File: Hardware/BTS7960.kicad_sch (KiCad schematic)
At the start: 29 parts, among them J10 Screw_Terminal_01x04, J11 Screw_Terminal_01x04, J4 Screw_Terminal_01x04, U7 HCPL-2631, U8 HCPL-2631

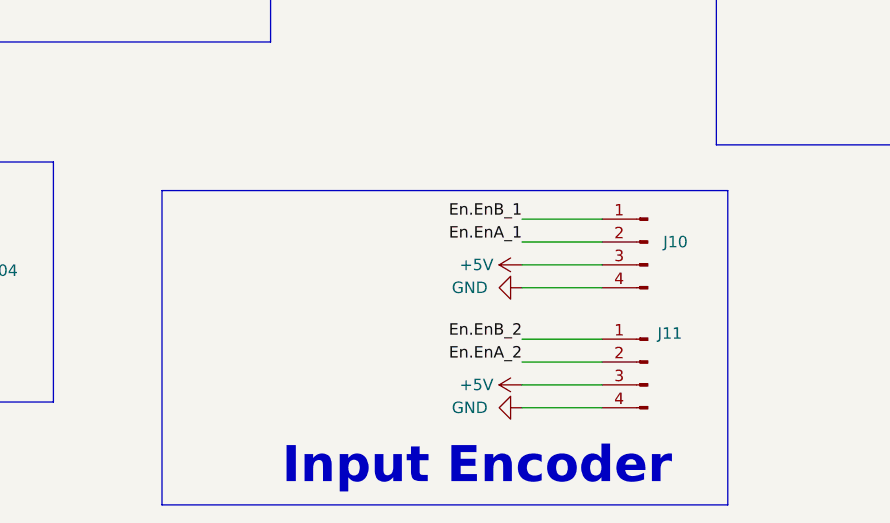
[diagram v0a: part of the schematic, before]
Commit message: Voltage divider and Update I2C PinHeader
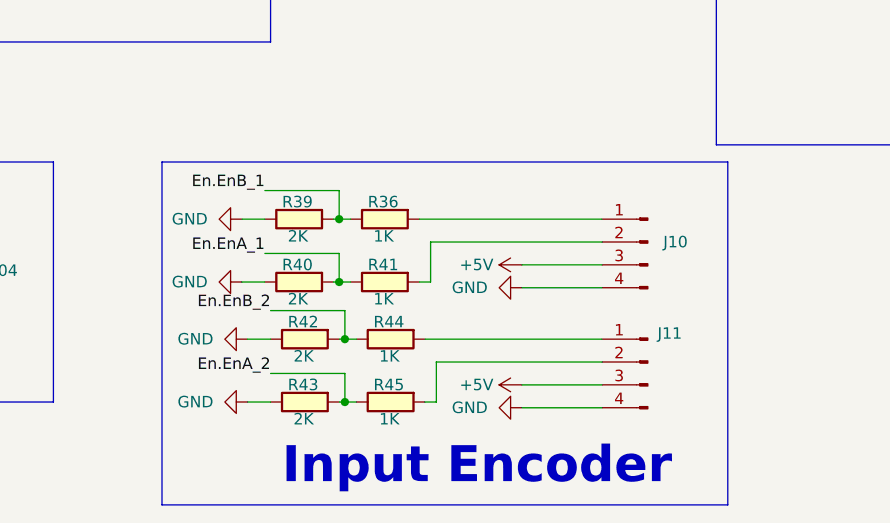
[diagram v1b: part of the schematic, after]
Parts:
- added R36, R41, R44, R45: 1K, IVS_FOOTPRINTS:R_0603, symbol IVS_SYMBOLS:R
- added R39, R40, R42, R43: 2K, IVS_FOOTPRINTS:R_0603, symbol IVS_SYMBOLS:R
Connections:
- net En.EnA_1: now also R40.1, R41.2; no longer J10.2 (Pin_2)
- net En.EnA_2: now also R43.1, R45.2; no longer J11.2 (Pin_2)
- net En.EnB_1: now also R36.2, R39.1; no longer J10.1 (Pin_1)
- net En.EnB_2: now also R42.1, R44.2; no longer J11.1 (Pin_1)
- net GND: now also R39.2, R40.2, R42.2, R43.2
- new net: J10.1 (Pin_1), R36.1
- new net: J10.2 (Pin_2), R41.1
- new net: J11.1 (Pin_1), R44.1
- new net: J11.2 (Pin_2), R45.1

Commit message: Layout track part 2
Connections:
- net Motor_L1: now also J4.3 (Pin_3); no longer J4.1 (Pin_1)
- net Motor_L2: now also J4.1 (Pin_1); no longer J4.3 (Pin_3)
- net Motor_R1: now also J4.4 (Pin_4); no longer J4.2 (Pin_2)
- net Motor_R2: now also J4.2 (Pin_2); no longer J4.4 (Pin_4)
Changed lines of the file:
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@@
     (effects (font (size 1.27 1.27)) (justify left bottom))
   )
-  (hierarchical_label "Motor_L1" (shape input) (at 50.165 163.195 180) (fields_autoplaced)
+  (hierarchical_label "Motor_L1" (shape input) (at 50.165 168.275 180) (fields_autoplaced)
     (effects (font (size 1.27 1.27)) (justify right))
   )
@@
     (effects (font (size 1.27 1.27)) (justify right))
   )
-  (hierarchical_label "Motor_R1" (shape input) (at 50.165 165.735 180) (fields_autoplaced)
+  (hierarchical_label "Motor_R1" (shape input) (at 50.165 170.815 180) (fields_autoplaced)
     (effects (font (size 1.27 1.27)) (justify right))
   )
@@
     (effects (font (size 1.27 1.27)) (justify left))
   )
-  (hierarchical_label "Motor_R2" (shape input) (at 50.165 170.815 180) (fields_autoplaced)
+  (hierarchical_label "Motor_R2" (shape input) (at 50.165 165.735 180) (fields_autoplaced)
     (effects (font (size 1.27 1.27)) (justify right))
   )
@@
     (effects (font (size 1.27 1.27)) (justify left))
   )
-  (hierarchical_label "Motor_L2" (shape input) (at 50.165 168.275 180) (fields_autoplaced)
+  (hierarchical_label "Motor_L2" (shape input) (at 50.165 163.195 180) (fields_autoplaced)
     (effects (font (size 1.27 1.27)) (justify right))
   )

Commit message: Complete layout board
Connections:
- net BTS.PWM_L1: now also R17.1; no longer R16.1
- net BTS.PWM_R1: now also R16.1; no longer R17.1
- net PWM_DC_L1: now also R18.2, U7.7 (VO1); no longer R19.2, U7.6 (VO2)
- net PWM_DC_R1: now also R19.2, U7.6 (VO2); no longer R18.2, U7.7 (VO1)
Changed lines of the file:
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@@
     (stroke (width 0) (type default))
   )
-  (wire (pts (xy 36.195 42.545) (xy 40.005 42.545))
+  (wire (pts (xy 34.925 42.545) (xy 40.005 42.545))
     (stroke (width 0) (type default))
   )
@@
     (stroke (width 0) (type default))
   )
-  (wire (pts (xy 36.195 57.785) (xy 40.005 57.785))
+  (wire (pts (xy 34.925 57.785) (xy 40.005 57.785))
     (stroke (width 0) (type default))
   )
@@
     (effects (font (size 1.27 1.27)) (justify left bottom))
   )
-  (label "PWM_DC_L1" (at 86.995 55.245 0) (fields_autoplaced)
+  (label "PWM_DC_L1" (at 78.105 45.085 0) (fields_autoplaced)
     (effects (font (size 1.27 1.27)) (justify left bottom))
   )
@@
     (effects (font (size 1.27 1.27)) (justify right bottom))
   )
-  (label "BTS.PWM_L1" (at 36.195 57.785 180) (fields_autoplaced)
+  (label "BTS.PWM_L1" (at 34.925 42.545 180) (fields_autoplaced)
     (effects (font (size 1.27 1.27)) (justify right bottom))
   )
@@
     (effects (font (size 1.27 1.27)) (justify right bottom))
   )
-  (label "PWM_DC_R1" (at 78.105 45.085 0) (fields_autoplaced)
+  (label "PWM_DC_R1" (at 86.995 55.245 0) (fields_autoplaced)
     (effects (font (size 1.27 1.27)) (justify left bottom))
   )
@@
     (effects (font (size 1.27 1.27)) (justify right bottom))
   )
-  (label "BTS.PWM_R1" (at 36.195 42.545 180) (fields_autoplaced)
-    (effects (font (size 1.27 1.27)) (justify right bottom))
-  )
+  (label "BTS.PWM_R1" (at 34.925 57.785 180) (fields_autoplaced)
+    (effects (font (size 1.27 1.27)) (justify right bottom))
+  )

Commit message: Update README
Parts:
- removed R36, R41: 1K, IVS_FOOTPRINTS:R_0603, symbol IVS_SYMBOLS:R
- removed R42, R43: 2K, IVS_FOOTPRINTS:R_0603, symbol IVS_SYMBOLS:R
- R39, R40: value 2K -> 10K
- R44, R45: value 1K -> 10K
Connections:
- net En.EnB_2 is gone; now on net En.EnA_2: R44.2
- net En.EnA_1: now also J10.2 (Pin_2), R39.2; no longer R40.1
- net En.EnA_2: now also J11.1 (Pin_1), J11.2 (Pin_2)
- net En.EnB_1: now also J10.1 (Pin_1), R40.2; no longer R39.1
- net GND: no longer R39.2, R40.2
- net +3V3_MCU: now reaches R44.1
- net +3V3_MCU: now also R39.1, R40.1, R45.1; no longer J11.1 (Pin_1)
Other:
- moved on the sheet: F3, J10, J11, R11, R44, R45, R7, U4
